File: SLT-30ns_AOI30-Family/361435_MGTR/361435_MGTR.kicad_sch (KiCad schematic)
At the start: 27 parts, among them T1 IBM_Transistor, T2 IBM_Transistor, T3 IBM_Transistor, T4 IBM_Transistor

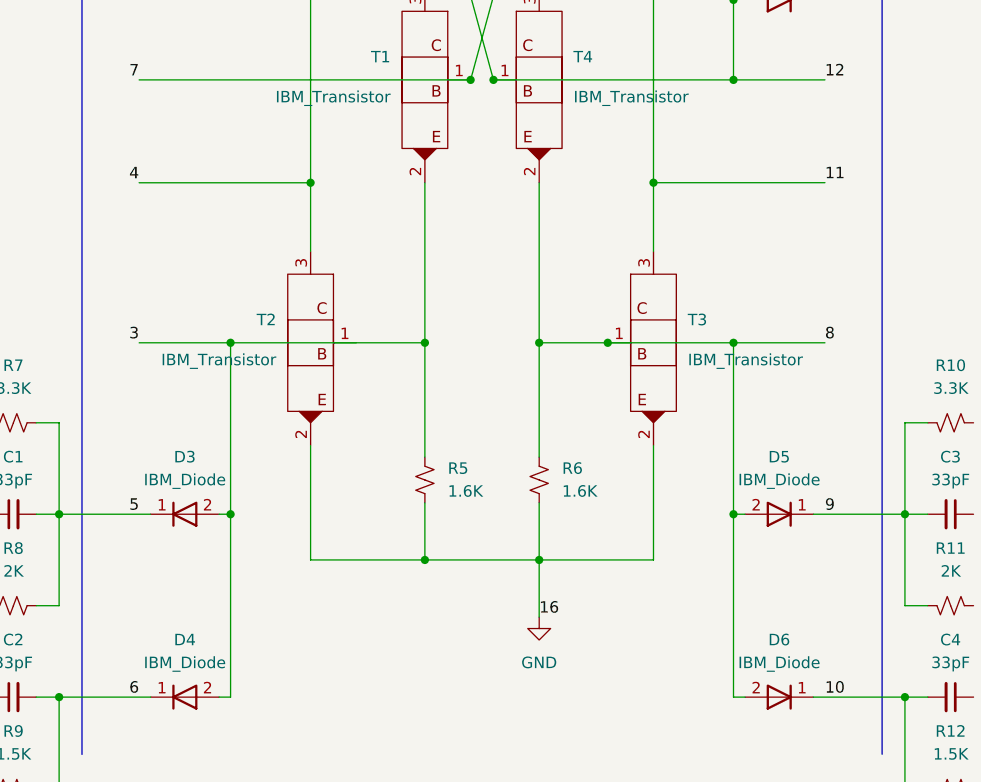
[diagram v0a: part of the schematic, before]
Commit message: Added labels for set/reset and +/- outputs
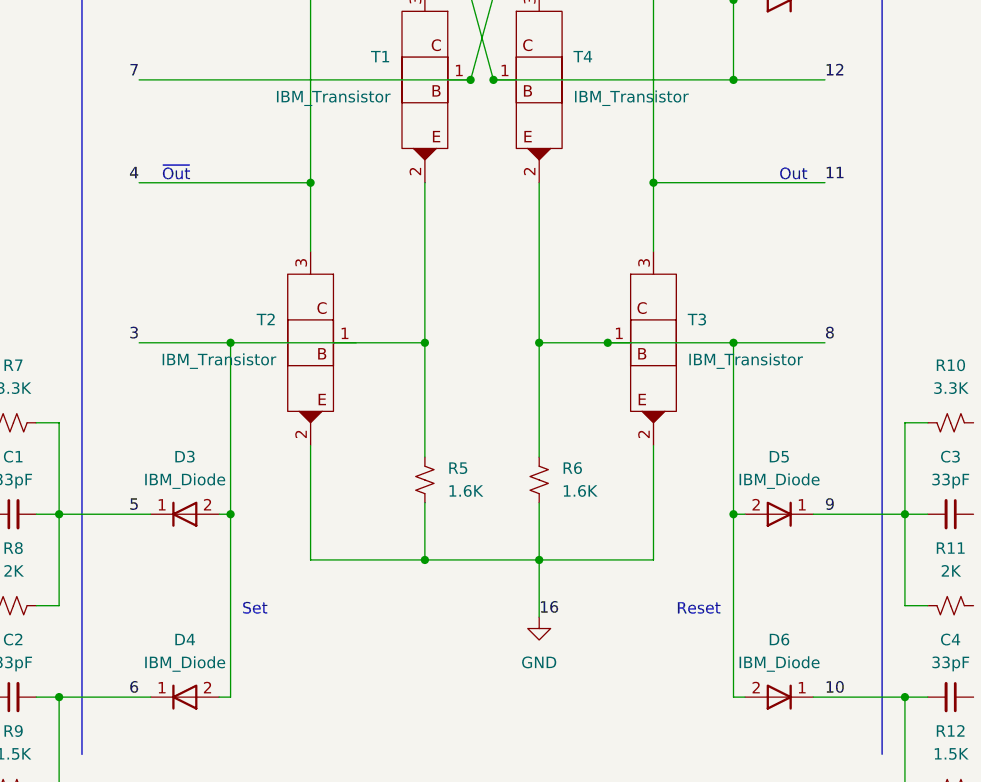
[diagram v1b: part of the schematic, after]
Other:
- note added: "Out"
- note added: "Reset"
- note added: "Set"
- note added: "~{Out}"
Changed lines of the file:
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@@
     (stroke (width 0) (type default) (color 0 0 0 0))
+  )
+  (text "~{Out}" (at 72.39 76.2 0)
+    (effects (font (size 1.27 1.27)) (justify left bottom))
+  )
+  (text "Out" (at 140.97 76.2 0)
+    (effects (font (size 1.27 1.27)) (justify left bottom))
+  )
+  (text "Reset" (at 129.54 124.46 0)
+    (effects (font (size 1.27 1.27)) (justify left bottom))
   )
   (text "All components outside of broken\nlines are external to module."
@@
     (effects (font (size 1.27 1.27)) (justify left bottom))
   )
+  (text "Set" (at 81.28 124.46 0)
+    (effects (font (size 1.27 1.27)) (justify left bottom))
+  )

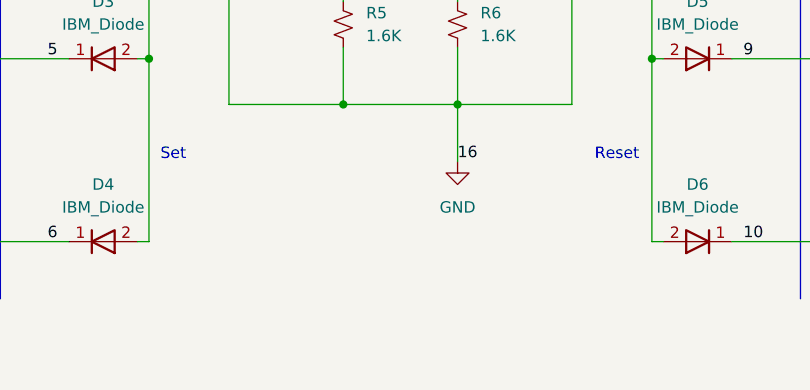
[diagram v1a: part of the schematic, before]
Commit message: Update schematic pdfs
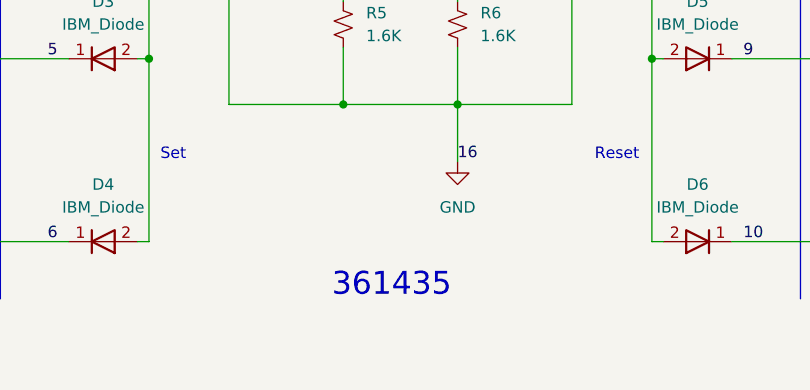
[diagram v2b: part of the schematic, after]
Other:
- note added: "361435"
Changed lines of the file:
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@@
     (effects (font (size 1.27 1.27)) (justify left bottom))
+  )
+  (text "361435" (at 100.33 139.7 0)
+    (effects (font (size 2.54 2.54)) (justify left bottom))
   )
   (text "Reset" (at 129.54 124.46 0)
